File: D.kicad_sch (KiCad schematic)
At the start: 11 parts

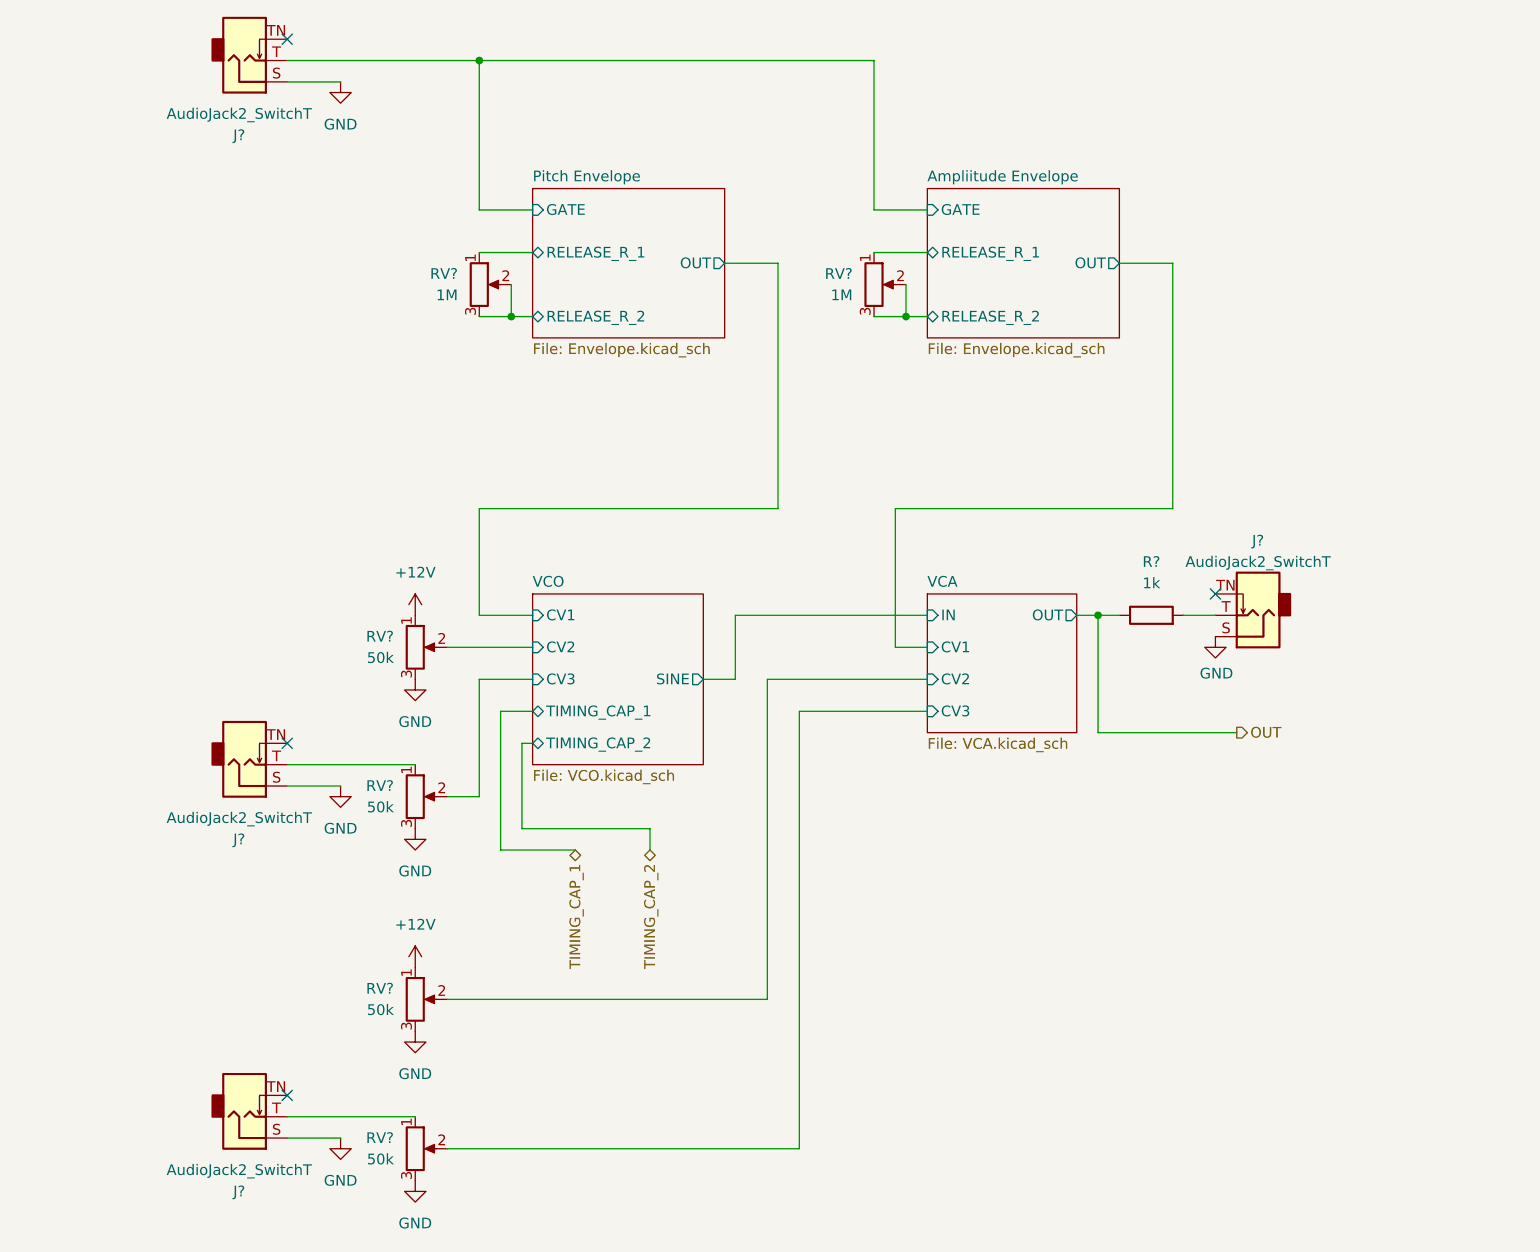
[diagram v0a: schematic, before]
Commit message: Finish schematic
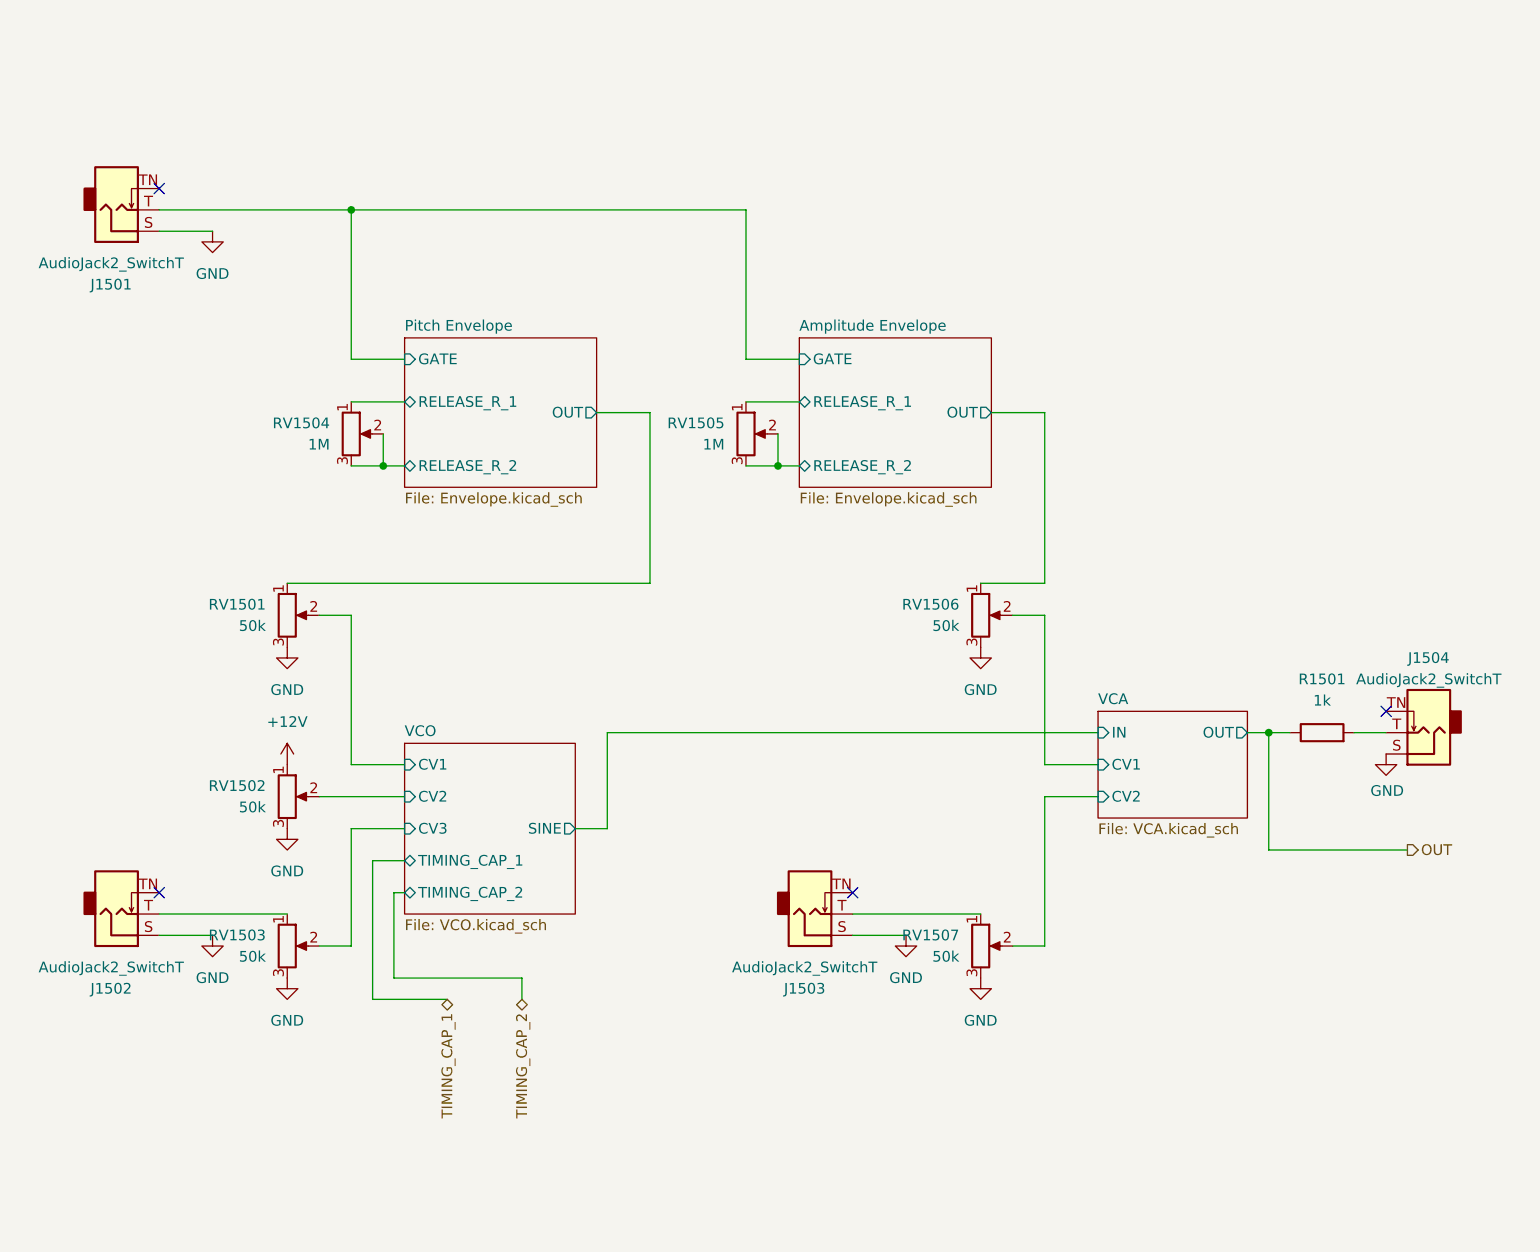
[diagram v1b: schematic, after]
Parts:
- removed J?: AudioJack2_SwitchT, symbol Connector:AudioJack2_SwitchT
- removed RV? (x2): 50k, symbol Device:R_Potentiometer
- added J1503: AudioJack2_SwitchT, Connector_Audio:Jack_3.5mm_QingPu_WQP-PJ398SM_Vertical_CircularHoles, symbol Connector:AudioJack2_SwitchT
- added RV1501, RV1506, RV1507: 50k, Potentiometer_THT:Potentiometer_Alpha_RD901F-40-00D_Single_Vertical_CircularHoles, symbol Device:R_Potentiometer
- J1501, J1502: renamed from J?; footprint (none) -> Connector_Audio:Jack_3.5mm_QingPu_WQP-PJ398SM_Vertical_CircularHoles
- R1501: renamed from R?; footprint (none) -> Resistor_THT:R_Axial_DIN0207_L6.3mm_D2.5mm_P7.62mm_Horizontal
- RV1502, RV1503, RV1504, RV1505: renamed from RV?; footprint (none) -> Potentiometer_THT:Potentiometer_Alpha_RD901F-40-00D_Single_Vertical_CircularHoles
- gave numbers to parts that had none: 1
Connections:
- net Amplitude Envelope/OUT: now also RV1506.1
- net GND: now also J1503.S, RV1501.3, RV1506.3, RV1507.3
- net Pitch Envelope/OUT: now also RV1501.1
- net VCA/CV2: now also RV1507.2
- new net: J1503.T, RV1507.1
- new net VCA/CV1: RV1506.2
- new net VCO/CV1: RV1501.2
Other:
- sheet Ampliitude Envelope renamed Amplitude Envelope
- sheet VCA ports: added none; removed CV3
- moved on the sheet: J1501, J1502, J1504, R1501, RV1502, RV1503, RV1504, RV1505

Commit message: Update VCO
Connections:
- net GND: no longer RV1502.3
- new net -12V: RV1502.3
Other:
- sheet VCO ports: added none; removed TIMING_CAP_1, TIMING_CAP_2
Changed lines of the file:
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@@
-    (stroke (width 0) (type default) (color 0 0 0 0))
-  )
-  (wire (pts (xy 105.41 143.51) (xy 114.3 143.51))
     (stroke (width 0) (type default) (color 0 0 0 0))
   )
@@
     (stroke (width 0) (type default) (color 0 0 0 0))
   )
-  (wire (pts (xy 123.19 140.97) (xy 123.19 143.51))
-    (stroke (width 0) (type default) (color 0 0 0 0))
-  )
   (wire (pts (xy 149.86 72.39) (xy 156.21 72.39))
     (stroke (width 0) (type default) (color 0 0 0 0))
@@
     (stroke (width 0) (type default) (color 0 0 0 0))
   )
-  (wire (pts (xy 109.22 130.81) (xy 107.95 130.81))
-    (stroke (width 0) (type default) (color 0 0 0 0))
-  )
   (wire (pts (xy 138.43 93.98) (xy 138.43 73.66))
     (stroke (width 0) (type default) (color 0 0 0 0))
@@
     (stroke (width 0) (type default) (color 0 0 0 0))
   )
-  (wire (pts (xy 105.41 127) (xy 105.41 143.51))
-    (stroke (width 0) (type default) (color 0 0 0 0))
-  )
   (wire (pts (xy 212.09 111.76) (xy 214.63 111.76))
     (stroke (width 0) (type default) (color 0 0 0 0))
@@
     (stroke (width 0) (type default) (color 0 0 0 0))
   )
-  (wire (pts (xy 109.22 127) (xy 105.41 127))
-    (stroke (width 0) (type default) (color 0 0 0 0))
-  )
   (wire (pts (xy 181.61 97.79) (xy 185.42 97.79))
     (stroke (width 0) (type default) (color 0 0 0 0))
@@
     (stroke (width 0) (type default) (color 0 0 0 0))
   )
-  (wire (pts (xy 107.95 140.97) (xy 123.19 140.97))
-    (stroke (width 0) (type default) (color 0 0 0 0))
-  )
   (wire (pts (xy 102.87 49.53) (xy 149.86 49.53))
     (stroke (width 0) (type default) (color 0 0 0 0))
@@
   )
   (wire (pts (xy 149.86 67.31) (xy 156.21 67.31))
-    (stroke (width 0) (type default) (color 0 0 0 0))
-  )
-  (wire (pts (xy 107.95 130.81) (xy 107.95 140.97))
     (stroke (width 0) (type default) (color 0 0 0 0))
   )
@@
   (hierarchical_label "OUT" (shape output) (at 228.6 125.73 0)
     (effects (font (size 1.27 1.27)) (justify left))
-  )
-  (hierarchical_label "TIMING_CAP_1" (shape bidirectional) (at 114.3 143.51 270)
-    (effects (font (size 1.27 1.27)) (justify right))
-  )
-  (hierarchical_label "TIMING_CAP_2" (shape bidirectional) (at 123.19 143.51 270)
-    (effects (font (size 1.27 1.27)) (justify right))
   )
   (symbol (lib_id "power:GND") (at 177.8 140.97 0)
@@
     (pin "3")
   )
+  (symbol (lib_id "power:-12V") (at 95.25 123.19 180)
+    (in_bom yes) (on_board yes) (fields_autoplaced)
+    (property "Reference" "#PWR01505" (id 0) (at 95.25 125.73 0)
+      (effects (font (size 1.27 1.27)) hide)
+    )
+    (property "Value" "-12V" (id 1) (at 95.25 128.27 0))
+    (property "Footprint" "" (id 2) (at 95.25 123.19 0)
+      (effects (font (size 1.27 1.27)) hide)
+    )
+    (property "Datasheet" "" (id 3) (at 95.25 123.19 0)
+      (effects (font (size 1.27 1.27)) hide)
+    )
+    (pin "1")
+  )
   (symbol (lib_id "power:GND") (at 86.36 52.07 0)
     (in_bom yes) (on_board yes) (fields_autoplaced)
@@
     (pin "TN")
   )
-  (symbol (lib_id "power:GND") (at 95.25 123.19 0)
-    (in_bom yes) (on_board yes) (fields_autoplaced)
-    (property "Reference" "#PWR01505" (id 0) (at 95.25 129.54 0)
-      (effects (font (size 1.27 1.27)) hide)
-    )
-    (property "Value" "GND" (id 1) (at 95.25 128.27 0))
-    (property "Footprint" "" (id 2) (at 95.25 123.19 0)
-      (effects (font (size 1.27 1.27)) hide)
-    )
-    (property "Datasheet" "" (id 3) (at 95.25 123.19 0)
-      (effects (font (size 1.27 1.27)) hide)
-    )
-    (pin "1")
-  )
   (symbol (lib_id "power:GND") (at 95.25 101.6 0)
     (in_bom yes) (on_board yes) (fields_autoplaced)
@@
     (pin "1")
   )
-  (sheet (at 109.22 113.03) (size 20.32 20.32) (fields_autoplaced)
+  (sheet (at 109.22 113.03) (size 20.32 12.7) (fields_autoplaced)
     (stroke (width 0.1524) (type solid) (color 0 0 0 0))
     (fill (color 0 0 0 0.0000))
@@
       (effects (font (size 1.27 1.27)) (justify left bottom))
     )
-    (property "Sheet file" "VCO.kicad_sch" (id 1) (at 109.22 133.9346 0)
+    (property "Sheet file" "VCO.kicad_sch" (id 1) (at 109.22 126.3146 0)
       (effects (font (size 1.27 1.27)) (justify left top))
     )
@@
       (effects (font (size 1.27 1.27)) (justify left))
     )
-    (pin "TIMING_CAP_1" bidirectional (at 109.22 127 180)
-      (effects (font (size 1.27 1.27)) (justify left))
-    )
-    (pin "TIMING_CAP_2" bidirectional (at 109.22 130.81 180)
-      (effects (font (size 1.27 1.27)) (justify left))
-    )
